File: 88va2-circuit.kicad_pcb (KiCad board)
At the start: 4 copper layers, 380 x 237.5 mm, 40 parts, among them CN2 FDD, CN4 TEXT BUS, CN5 LED, IC1 D65101GD055, IC13 SN74ALS374N, IC20 7407, IC21 uPD4990AC, IC22 DIP-14_W7.62mm, IC65 D65101GD110, IC9 D65200GD076, X2 32.768K

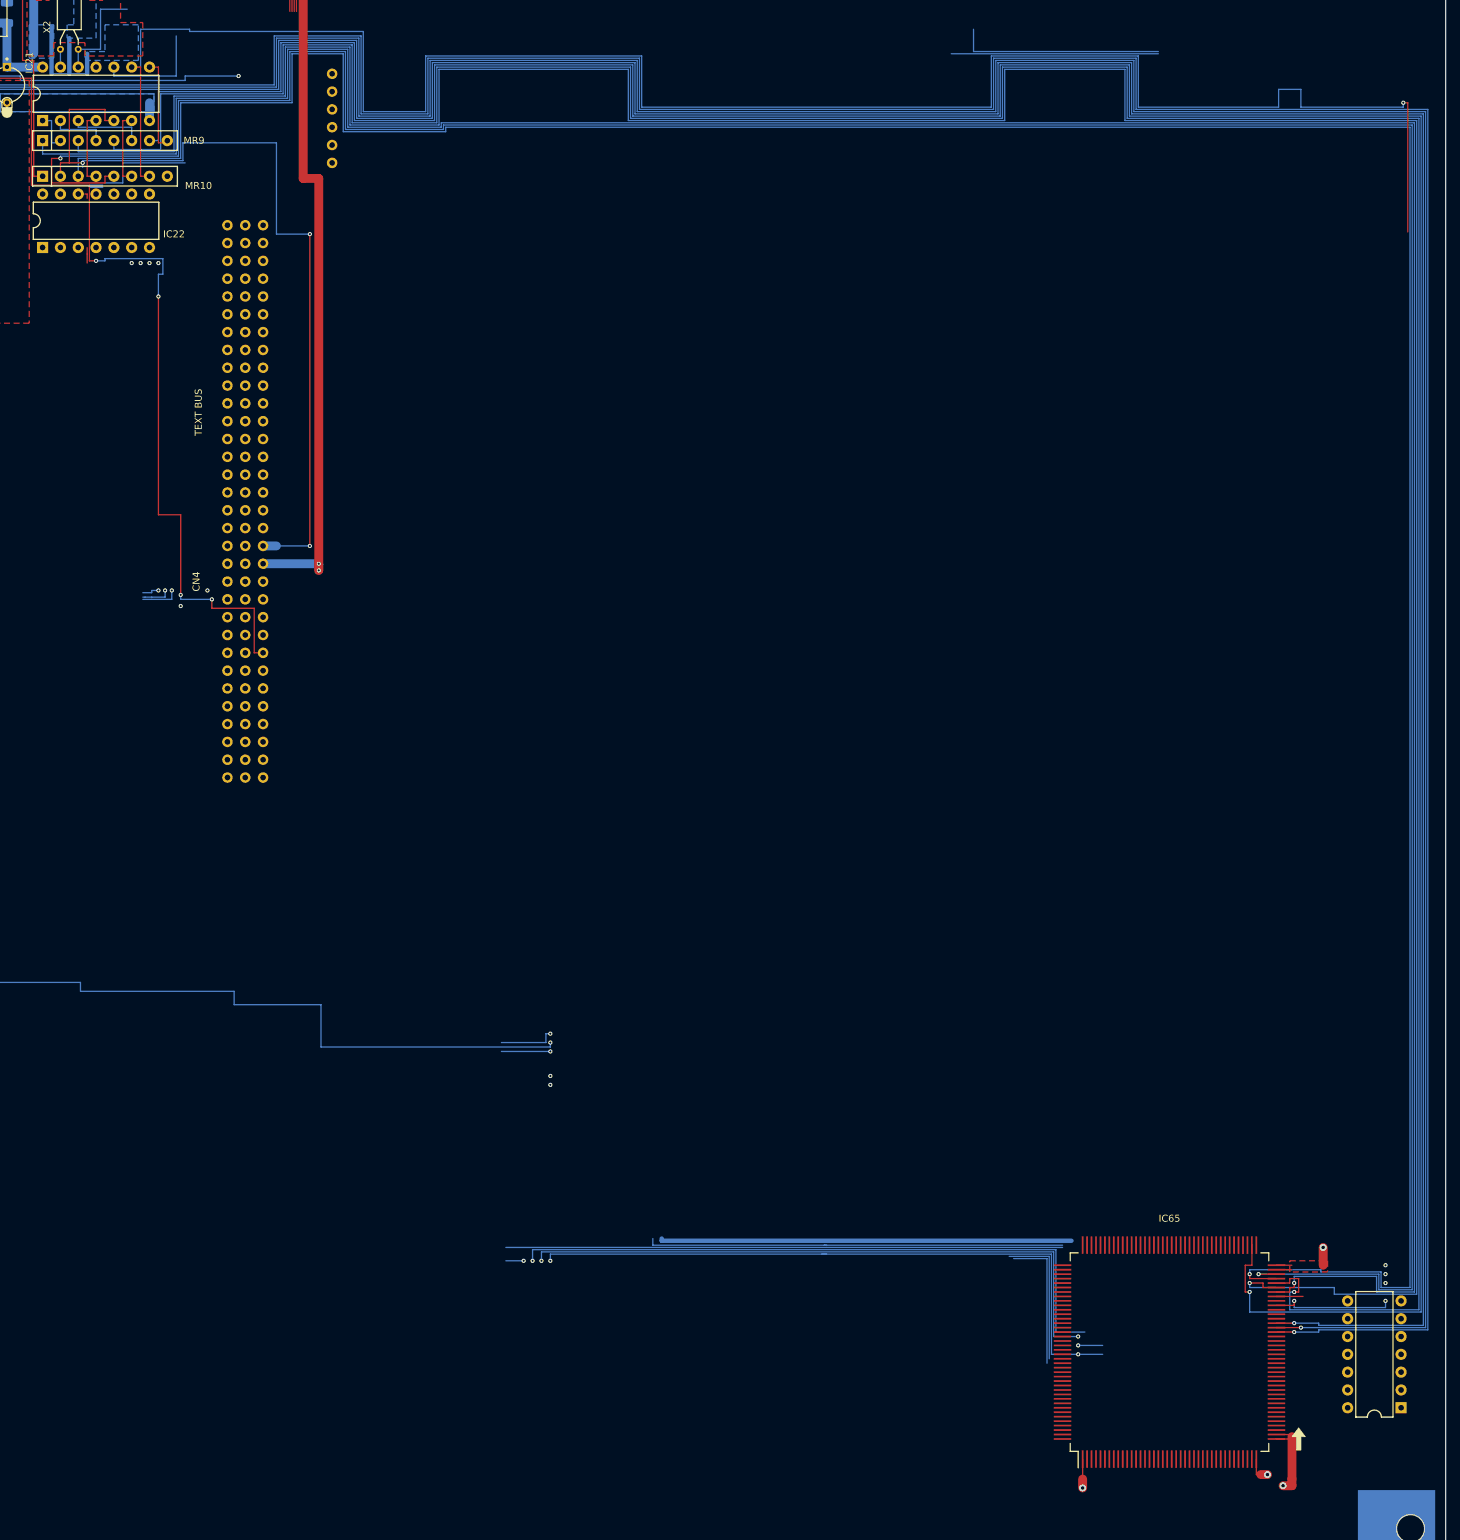
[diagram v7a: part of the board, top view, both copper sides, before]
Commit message: fix pitch of IC65 pads
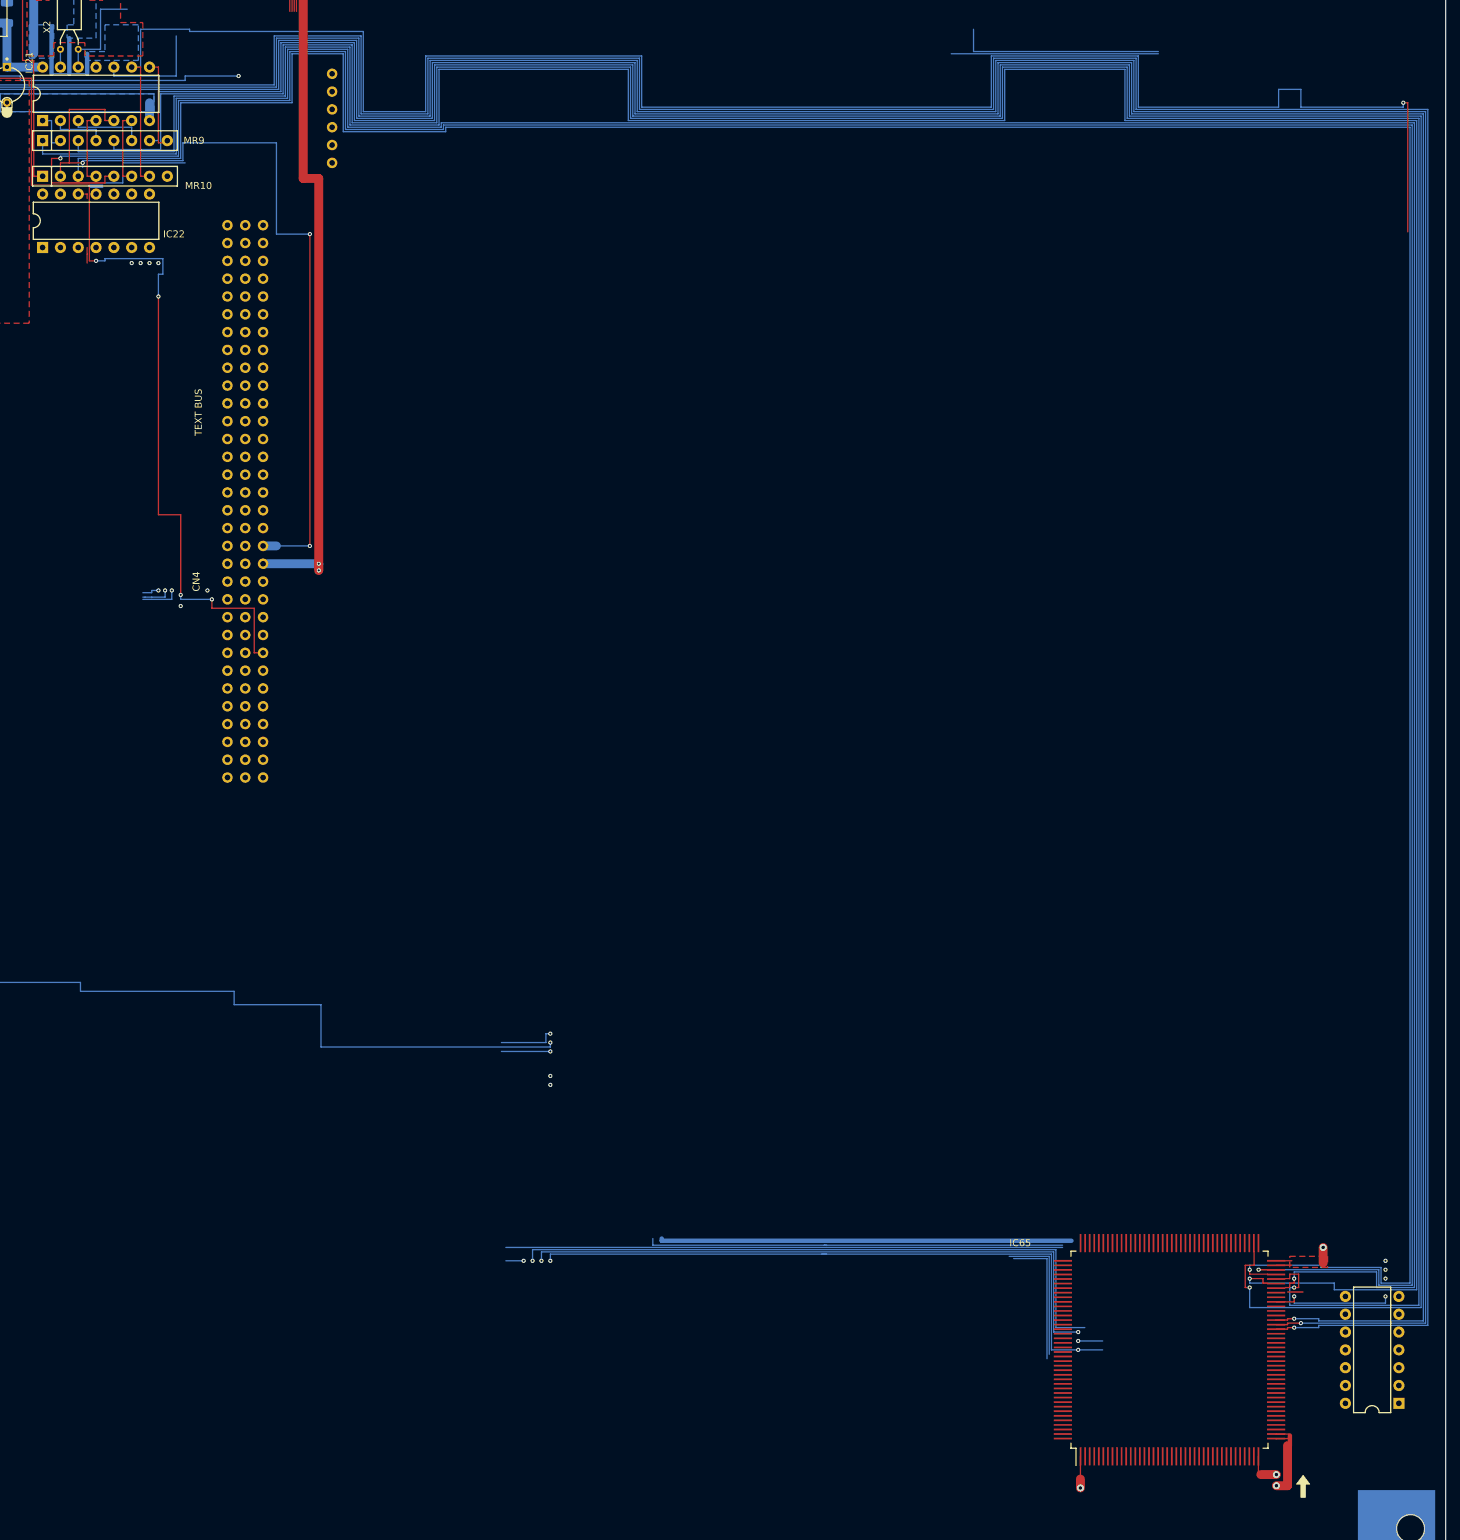
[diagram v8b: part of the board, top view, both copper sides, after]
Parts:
- added REF**: GAL_mark, 88va_Library:GAL_mark, F.Cu at (372.4, 241.4)
- IC65: footprint 88va_Library:QFP-160_28x28_Pitch0.635mm -> 88va_Library:QFP-160_27.8x27.8_Pitch0.65mm
- moved REF** 0.71 mm to (386.0, 231.1)
- moved IC65 0.34 mm to (353.3, 223.5)
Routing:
- net (no net): track 2455.7 -> 2451.6 mm
- net +5V: track 853.6 -> 856.7 mm
- net C0: track 441.0 -> 438.8 mm
- net CCLK: track 442.3 -> 440.4 mm
- net CDO: track 427.0 -> 425.1 mm
- net CSTB: track 415.2 -> 413.3 mm
- net C1: track 445.1 -> 443.2 mm
- net C2: track 414.6 -> 412.8 mm
- net Net-(IC65-XARESET?): track 303.2 -> 302.6 mm
